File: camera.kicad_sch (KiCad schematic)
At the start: 39 parts, among them J0 Conn_01x05_Male, J1 Conn_01x05_Male, J2 Conn_01x05_Male, J3 Conn_01x05_Male, J4 Conn_Coaxial, U1 HEF4051BT, U3 RTC6705, U4 SE5005L, Y3 8MHz

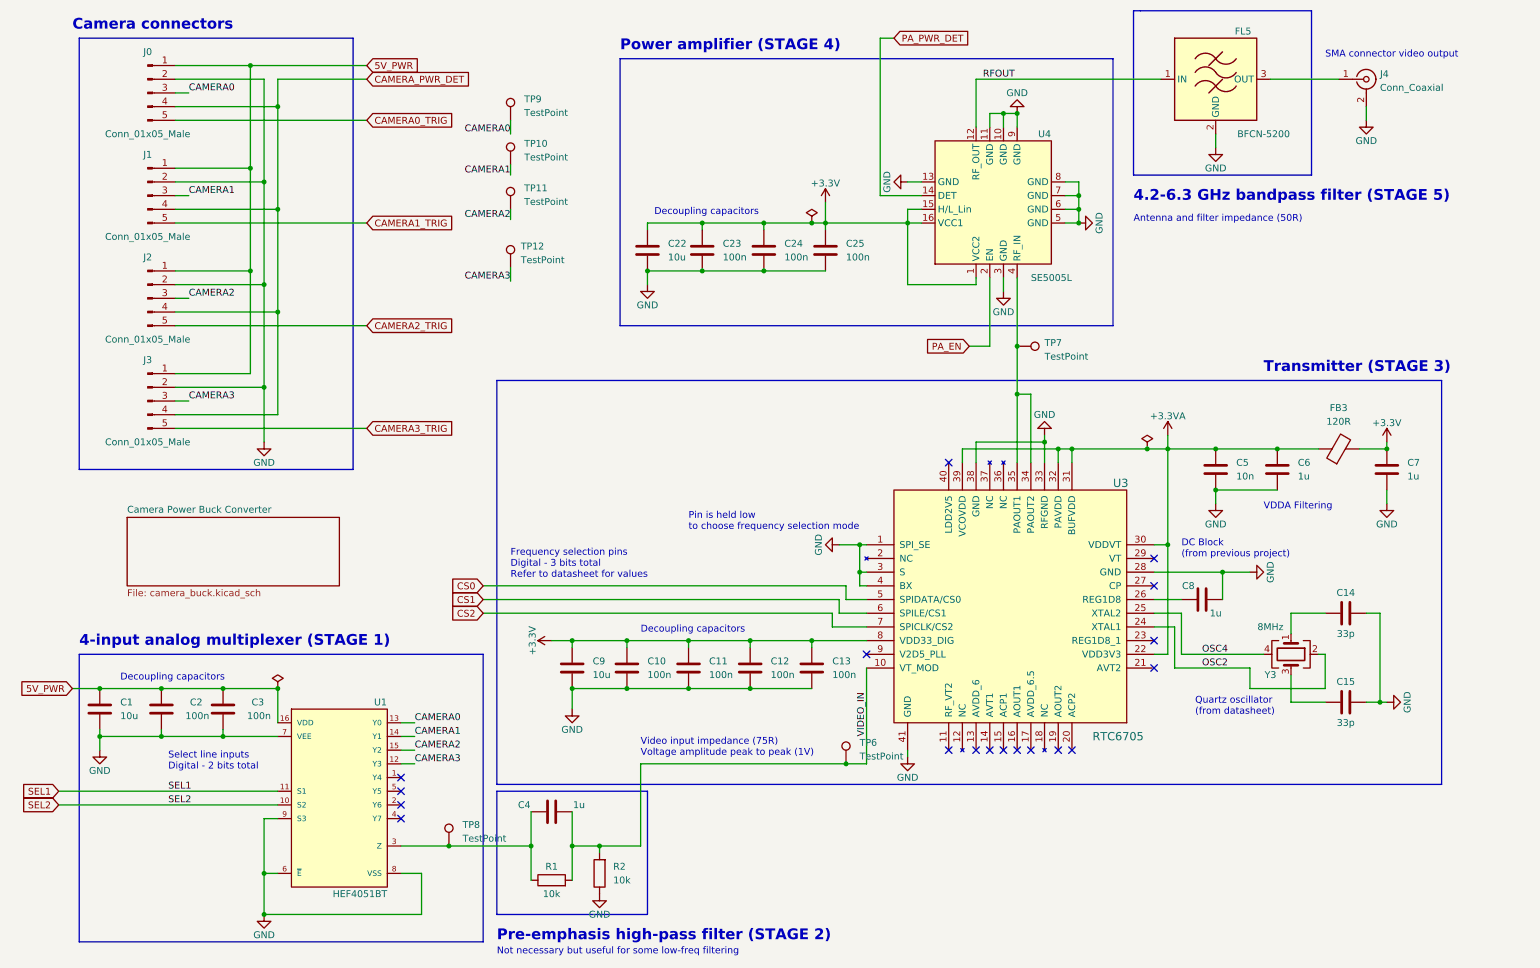
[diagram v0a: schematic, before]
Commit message: File names and ERC
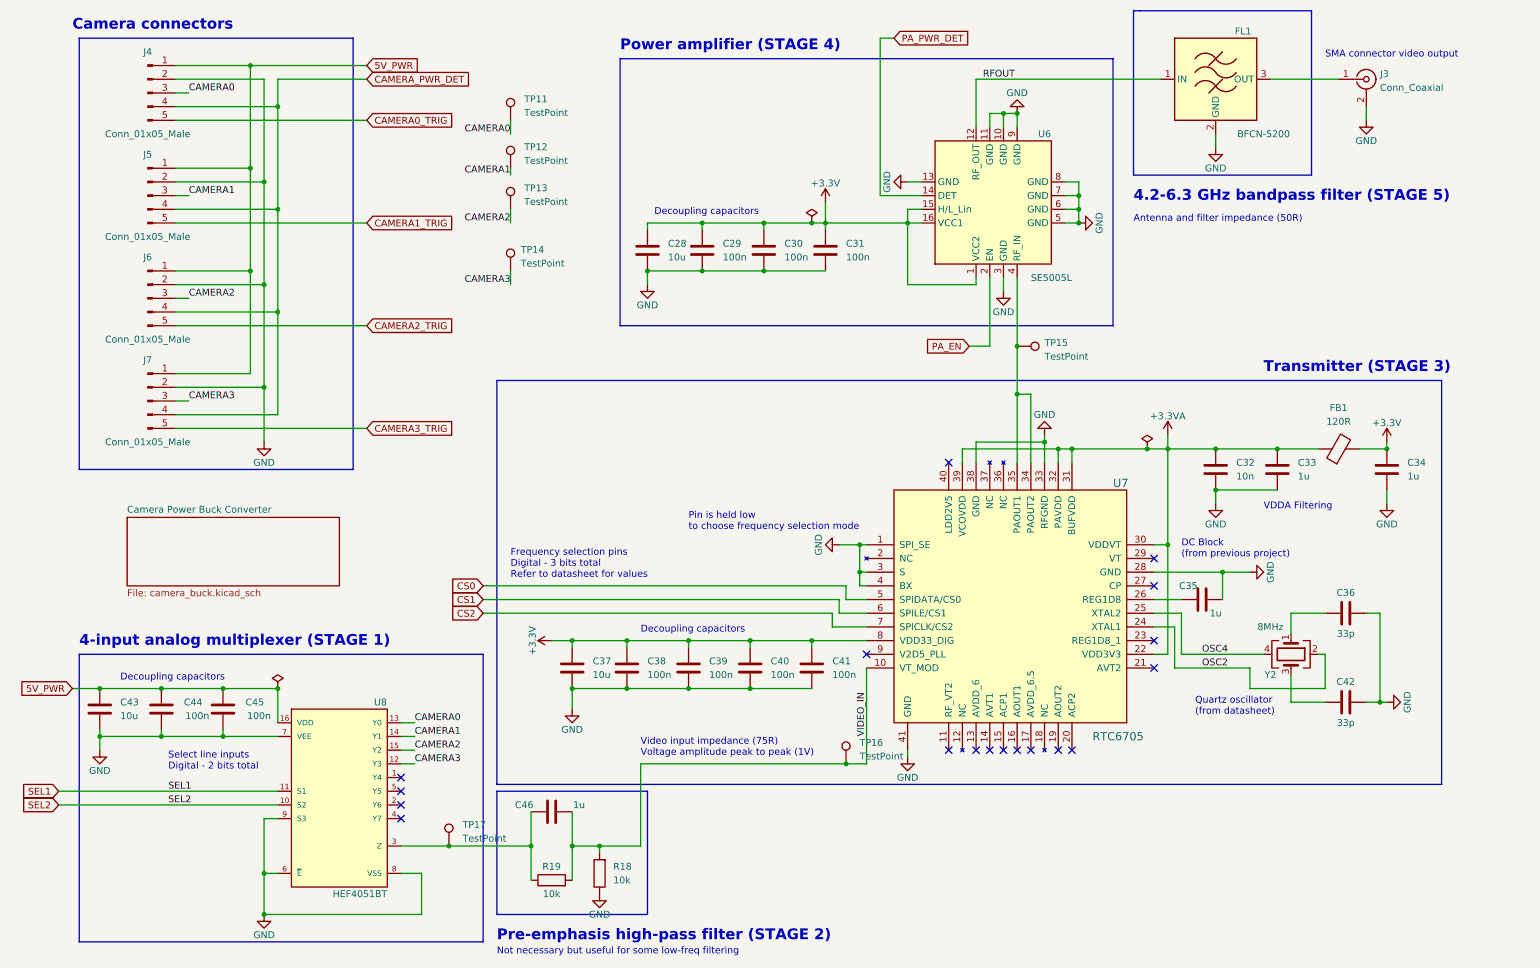
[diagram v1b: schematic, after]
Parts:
- renumbered C22 to C28, C23 to C29, C24 to C30, C25 to C31, C5 to C32, C6 to C33, C7 to C34, C8 to C35, C14 to C36, C9 to C37, C10 to C38, C11 to C39, C12 to C40, C13 to C41, C15 to C42, C1 to C43, C2 to C44, C3 to C45, C4 to C46, FB3 to FB1, FL5 to FL1, J4 to J3, J0 to J4, J1 to J5, J2 to J6, J3 to J7, R2 to R18, R1 to R19, TP9 to TP11, TP10 to TP12, TP11 to TP13, TP12 to TP14, TP7 to TP15, TP6 to TP16, TP8 to TP17, U4 to U6, U3 to U7, U1 to U8, Y3 to Y2
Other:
- moved on the sheet: TP12, TP14

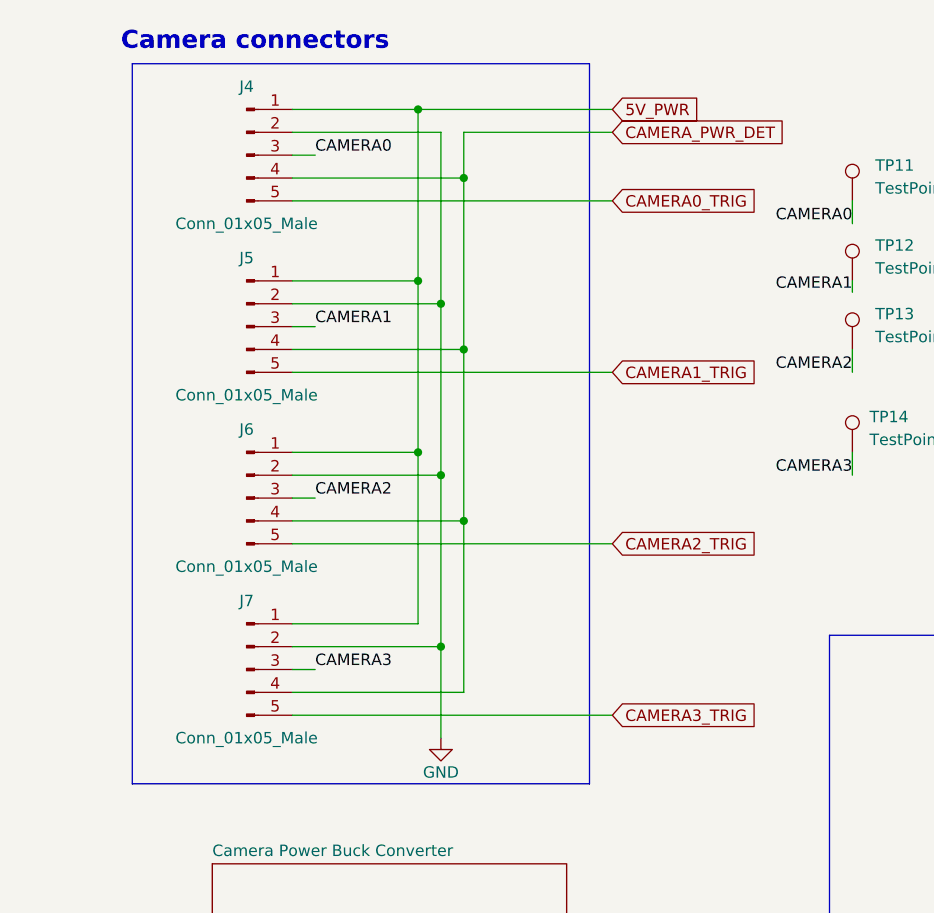
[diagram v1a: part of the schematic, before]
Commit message: Add photo triggers
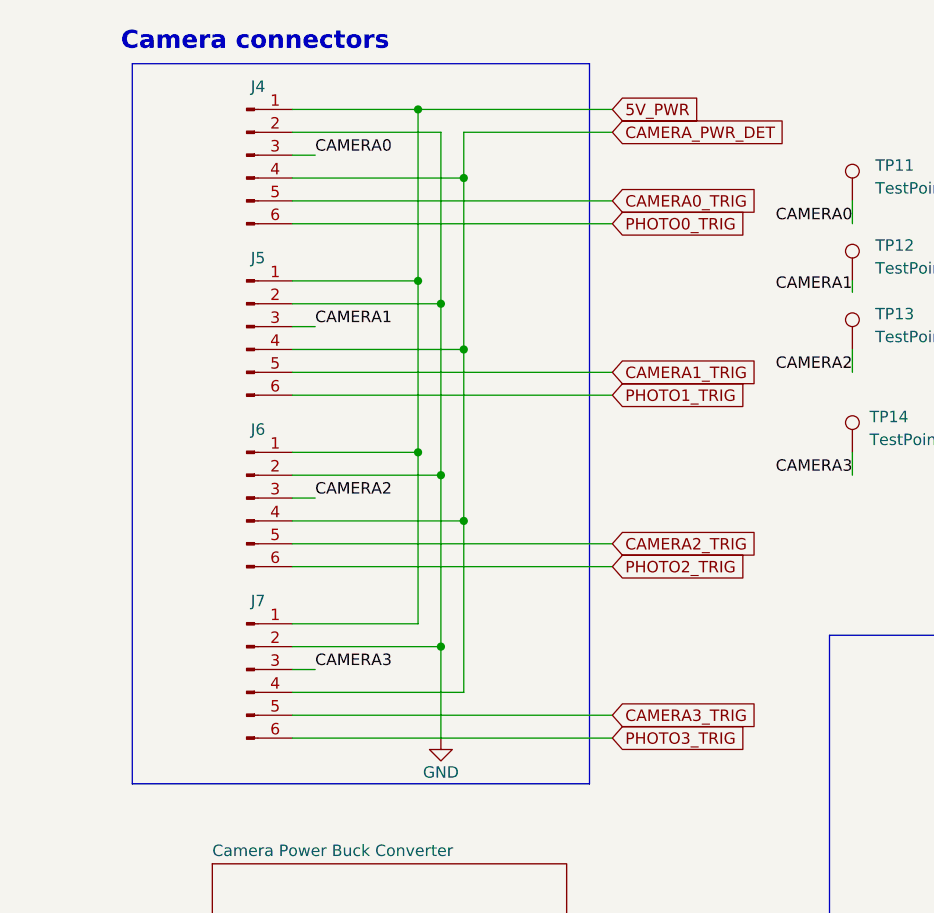
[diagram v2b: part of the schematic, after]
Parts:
- removed J4, J5, J6, J7: Conn_01x05_Male, Connector_JST:JST_XH_S6B-XH-A-1_1x06_P2.50mm_Horizontal, symbol Connector:Conn_01x05_Male
- added J4, J5, J6, J7: Conn_01x06_Pin, symbol Connector:Conn_01x06_Pin
- J3: footprint Diode_SMD:D_SMA -> Connector_Coaxial:SMA_Amphenol_901-144_Vertical
- U6: footprint iclr:QFN300X300X100-16N -> fps:QFN300X300X100-16N
- U7: footprint Custom:RTC6705 -> Ricardo-CHEESE:RTC6705
- U8: footprint HEF4051BT:SOIC127P600X175-16N -> Ricardo-CHEESE:SOIC127P600X175-16N
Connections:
- net 5V_PWR: now also J4.1 (Pin_1), J5.1 (Pin_1), J6.1 (Pin_1), J7.1 (Pin_1)
- net CAMERA0: now also J4.3 (Pin_3)
- net CAMERA0_TRIG: now also J4.5 (Pin_5)
- net CAMERA1: now also J5.3 (Pin_3)
- net CAMERA1_TRIG: now also J5.5 (Pin_5)
- net CAMERA2: now also J6.3 (Pin_3)
- net CAMERA2_TRIG: now also J6.5 (Pin_5)
- net CAMERA3: now also J7.3 (Pin_3)
- net CAMERA3_TRIG: now also J7.5 (Pin_5)
- net CAMERA_PWR_DET: now also J4.4 (Pin_4), J5.4 (Pin_4), J6.4 (Pin_4), J7.4 (Pin_4)
- net GND: now also J4.2 (Pin_2), J5.2 (Pin_2), J6.2 (Pin_2), J7.2 (Pin_2)
- new net PHOTO0_TRIG: J4.6 (Pin_6)
- new net PHOTO1_TRIG: J5.6 (Pin_6)
- new net PHOTO2_TRIG: J6.6 (Pin_6)
- new net PHOTO3_TRIG: J7.6 (Pin_6)

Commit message: Fixed libraries and footprints
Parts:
- added R26, R27, R28, R29, R30, R31, R32, R33, R34, R35: 1k, Resistor_SMD:R_0402_1005Metric, symbol Device:R
- J3: footprint Connector_Coaxial:SMA_Amphenol_901-144_Vertical -> Connector_Coaxial:SMA_Molex_73251-1153_EdgeMount_Horizontal
- J4, J5, J6, J7: footprint (none) -> Connector_JST:JST_PH_S6B-PH-K_1x06_P2.00mm_Horizontal
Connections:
- net 5V_PWR: now also R26.2; no longer J4.1 (Pin_1), J5.1 (Pin_1), J6.1 (Pin_1), J7.1 (Pin_1)
- net CAMERA0_TRIG: now also R28.2; no longer J4.5 (Pin_5)
- net CAMERA1_TRIG: now also R30.2; no longer J5.5 (Pin_5)
- net CAMERA2_TRIG: now also R32.2; no longer J6.5 (Pin_5)
- net CAMERA3_TRIG: now also R34.2; no longer J7.5 (Pin_5)
- net CAMERA_PWR_DET: now also R27.2; no longer J4.4 (Pin_4), J5.4 (Pin_4), J6.4 (Pin_4), J7.4 (Pin_4)
- net PHOTO0_TRIG: now also R29.2; no longer J4.6 (Pin_6)
- net PHOTO1_TRIG: now also R31.2; no longer J5.6 (Pin_6)
- net PHOTO2_TRIG: now also R33.2; no longer J6.6 (Pin_6)
- net PHOTO3_TRIG: now also R35.2; no longer J7.6 (Pin_6)
- new net: J7.5 (Pin_5), R34.1
- new net: J5.6 (Pin_6), R31.1
- new net: J6.6 (Pin_6), R33.1
- new net: J4.6 (Pin_6), R29.1
- new net: J4.1 (Pin_1), J5.1 (Pin_1), J6.1 (Pin_1), J7.1 (Pin_1), R26.1
- new net: J4.4 (Pin_4), J5.4 (Pin_4), J6.4 (Pin_4), J7.4 (Pin_4), R27.1
- new net: J4.5 (Pin_5), R28.1
- new net: J6.5 (Pin_5), R32.1
- new net: J7.6 (Pin_6), R35.1
- new net: J5.5 (Pin_5), R30.1

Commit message: Some routing
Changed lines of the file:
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@@
     )
   )
-  (symbol (lib_id "Device:C") (at 161.29 138.43 0) (unit 1)
-    (in_bom yes) (on_board yes) (dnp no) (fields_autoplaced)
-    (property "Reference" "C41" (at 165.1 137.1599 0)
+  (symbol (lib_id "Device:C") (at 161.29 138.43 0) (mirror y) (unit 1)
+    (in_bom yes) (on_board yes) (dnp no)
+    (property "Reference" "C41" (at 157.48 137.1599 0)
       (effects (font (size 1.27 1.27)) (justify left))
     )
-    (property "Value" "100n" (at 165.1 139.6999 0)
+    (property "Value" "100n" (at 157.48 139.6999 0)
       (effects (font (size 1.27 1.27)) (justify left))
     )
-    (property "Footprint" "Capacitor_SMD:C_0402_1005Metric" (at 162.2552 142.24 0)
+    (property "Footprint" "Capacitor_SMD:C_0402_1005Metric" (at 160.3248 142.24 0)
       (effects (font (size 1.27 1.27)) hide)
     )

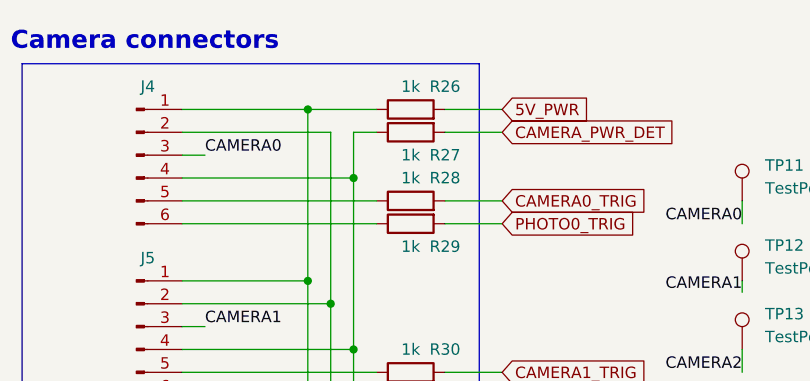
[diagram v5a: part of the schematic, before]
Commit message: Camera buck changes, c and r footprints, other
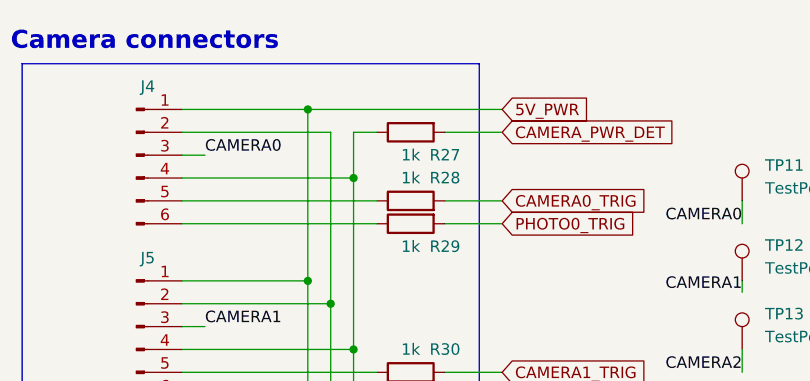
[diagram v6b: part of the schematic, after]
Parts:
- removed R26: 1k, Resistor_SMD:R_0402_1005Metric, symbol Device:R
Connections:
- net 5V_PWR: now also J4.1 (Pin_1), J5.1 (Pin_1), J6.1 (Pin_1), J7.1 (Pin_1)
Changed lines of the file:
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@@
     (stroke (width 0) (type default))
   )
-  (wire (pts (xy 72.39 26.67) (xy 78.74 26.67))
+  (wire (pts (xy 57.15 26.67) (xy 78.74 26.67))
     (stroke (width 0) (type default))
   )
@@
   )
   (wire (pts (xy 43.18 36.83) (xy 64.77 36.83))
-    (stroke (width 0) (type default))
-  )
-  (wire (pts (xy 57.15 26.67) (xy 64.77 26.67))
     (stroke (width 0) (type default))
   )
@@
         )
       )
-    )
-  )
-  (symbol (lib_id "Device:R") (at 68.58 26.67 90) (unit 1)
-    (in_bom yes) (on_board yes) (dnp no)
-    (property "Reference" "R26" (at 72.39 24.13 90)
-      (effects (font (size 1.27 1.27)))
-    )
-    (property "Value" "1k" (at 68.58 24.13 90)
-      (effects (font (size 1.27 1.27)))
-    )
-    (property "Footprint" "Resistor_SMD:R_0402_1005Metric" (at 68.58 28.448 90)
-      (effects (font (size 1.27 1.27)) hide)
-    )
-    (property "Datasheet" "~" (at 68.58 26.67 0)
-      (effects (font (size 1.27 1.27)) hide)
-    )
-    (pin "1")
-    (pin "2")
-    (instances
-      (project "RicardoCHEESE"
-        (path "/7db990e4-92e1-4f99-b4d2-435bbec1ba83/90cb145e-dae6-40dc-8720-fcf8047ab530"
-          (reference "R26") (unit 1)
-        )
-      )

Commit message: Footprinting and board outline
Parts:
- C28, C33, C34, C35: footprint Capacitor_SMD:C_0603_1608Metric -> Capacitor_SMD:C_0402_1005Metric
- FB1: footprint Inductor_SMD:L_0603_1608Metric -> Inductor_SMD:L_0402_1005Metric
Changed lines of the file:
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@@
       (effects (font (size 1.27 1.27)) (justify left))
     )
-    (property "Footprint" "Capacitor_SMD:C_0603_1608Metric" (at 131.7752 64.77 0)
+    (property "Footprint" "Capacitor_SMD:C_0402_1005Metric" (at 131.7752 64.77 0)
       (effects (font (size 1.27 1.27)) hide)
     )
@@
       (effects (font (size 1.27 1.27)))
     )
-    (property "Footprint" "Inductor_SMD:L_0603_1608Metric" (at 259.08 99.568 90)
+    (property "Footprint" "Inductor_SMD:L_0402_1005Metric" (at 259.08 99.568 90)
       (effects (font (size 1.27 1.27)) hide)
     )
@@
       (effects (font (size 1.27 1.27)) (justify left))
     )
-    (property "Footprint" "Capacitor_SMD:C_0603_1608Metric" (at 248.6152 105.41 0)
+    (property "Footprint" "Capacitor_SMD:C_0402_1005Metric" (at 248.6152 105.41 0)
       (effects (font (size 1.27 1.27)) hide)
     )
@@
       (effects (font (size 1.27 1.27)))
     )
-    (property "Footprint" "Capacitor_SMD:C_0603_1608Metric" (at 237.49 124.7648 0)
+    (property "Footprint" "Capacitor_SMD:C_0402_1005Metric" (at 237.49 124.7648 0)
       (effects (font (size 1.27 1.27)) hide)
     )
@@
       (effects (font (size 1.27 1.27)) (justify left))
     )
-    (property "Footprint" "Capacitor_SMD:C_0603_1608Metric" (at 268.9352 105.41 0)
-      (effects (font (size 1.27 1.27)) hide)
-    )
+    (property "Footprint" "Capacitor_SMD:C_0402_1005Metric" (at 268.9352 105.41 0)
+      (effects (font (size 1.27 1.27)) hide)
+    )
